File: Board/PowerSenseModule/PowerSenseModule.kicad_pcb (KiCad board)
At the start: 2 copper layers, 49 parts, among them J1 Conn_01x06_Male, J3 Programming Header, J4 Conn_01x02_Male, U1 TPS82150, U2 NCV2007x, U3 dsPIC33EV32GM102, U4 MCP2542FDxMF

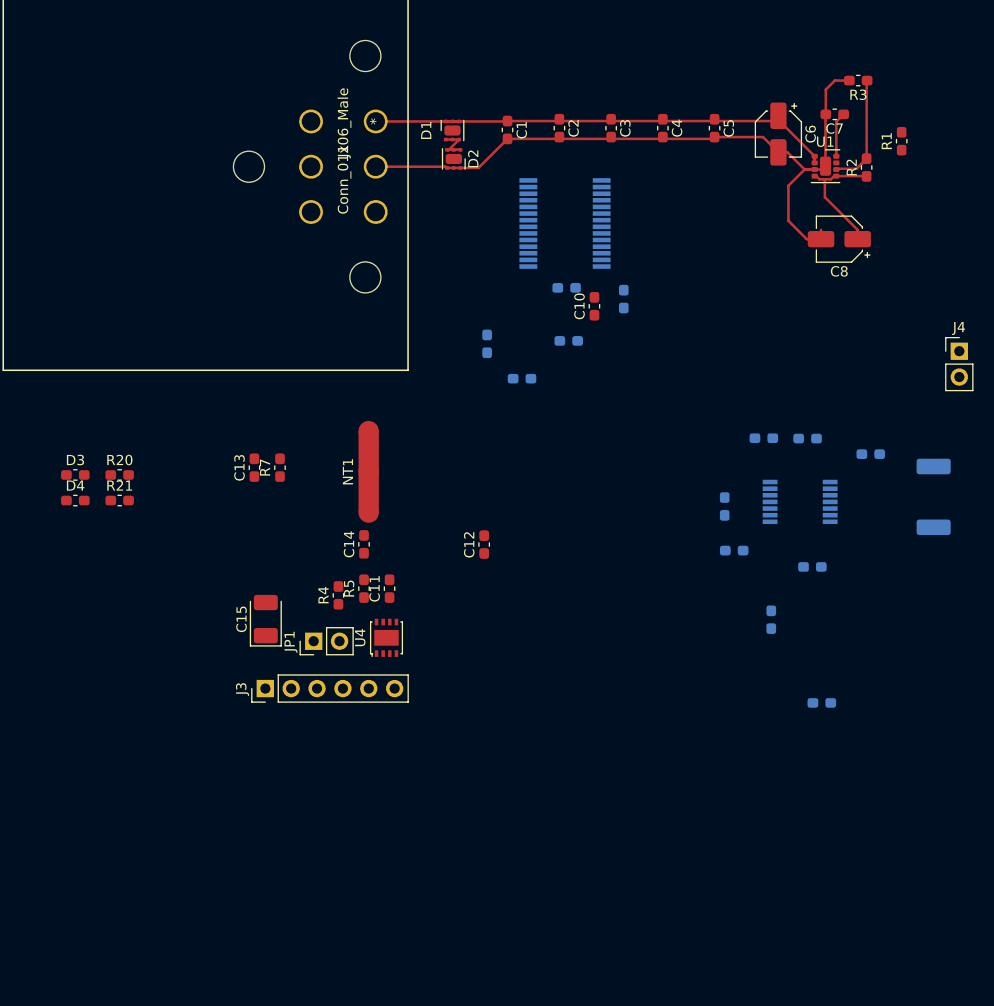
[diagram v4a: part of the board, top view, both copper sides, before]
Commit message: Added to PCB layout - Configurations Resistor / PIN 3 mapping
More of the PCB is laid out. Some mapping remains. Aside from that, what's left is the following, 
- Assuring PCB traces meet current limitations 
- Design review for optimizations for redesign. 
Alongside that, the configuration resistors do not seem to be connected to PIN 3 on the MCU.
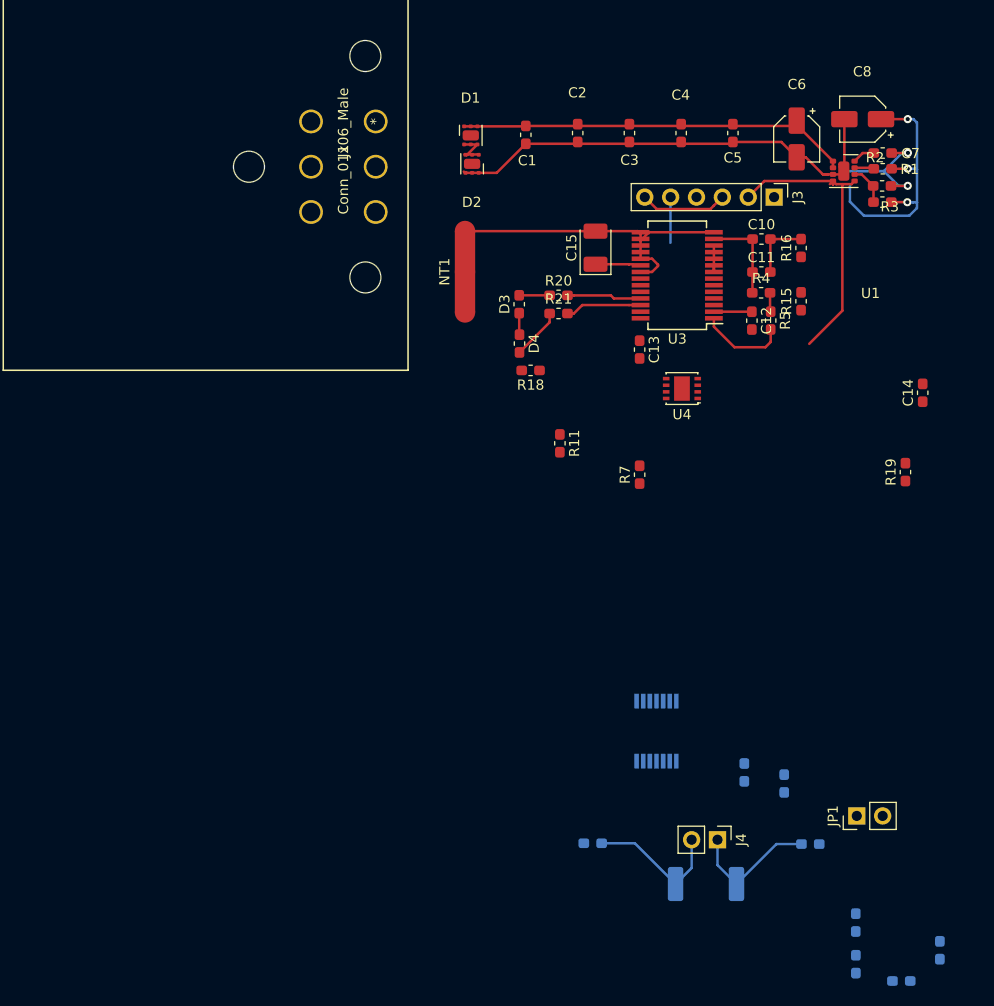
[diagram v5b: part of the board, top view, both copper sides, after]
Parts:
- R11, R15, R16, R18, R19, U3: moved to F.Cu
- moved R17 72.3 mm to (145.3, 168.6), turned to 180 degrees
- moved J3 69.5 mm to (132.8, 91.6), turned to 270 degrees
- moved C14 56.8 mm to (147.4, 110.8)
- moved JP1 56.0 mm to (140.9, 152.3)
- moved J4 53.5 mm to (127.2, 154.7), turned to 270 degrees
- moved R14 51.9 mm to (149.1, 165.5), turned to 90 degrees
- moved R4 51.0 mm to (131.5, 101.0), turned to 0 degrees
- moved C15 48.8 mm to (115.3, 96.5)
- moved R13 48.4 mm to (140.8, 162.8), turned to 270 degrees
- moved C11 48.0 mm to (131.6, 98.9), turned to 0 degrees
- moved R5 47.8 mm to (132.5, 103.7), turned to 270 degrees
- moved R21 46.8 mm to (111.6, 103.0)
- moved D3 46.7 mm to (107.8, 102.1), turned to 90 degrees
- moved R20 46.6 mm to (111.6, 101.2)
- moved D4 46.3 mm to (107.8, 106.0), turned to 270 degrees
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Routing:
- net +5V: track 12.6 -> 64.4 mm, vias 0 -> 3
- net GNDD: track 0.00 -> 51.6 mm
- net Net-(J4-Pad2): track 0.00 -> 14.0 mm
- net Net-(J4-Pad1): track 0.00 -> 13.2 mm
- net Net-(R5-Pad2): track 0.00 -> 8.67 mm
- net GND: track 68.1 -> 59.5 mm, vias 0 -> 2
- net +12V: track 46.8 -> 38.6 mm
- net Net-(R21-Pad2): track 0.00 -> 7.52 mm
- net Net-(R20-Pad2): track 0.00 -> 7.30 mm
- net Net-(R2-Pad2): track 11.1 -> 4.00 mm
- net Net-(D4-Pad2): track 0.00 -> 5.05 mm
- net Net-(J3-Pad5): track 0.00 -> 4.46 mm, vias 0 -> 1
- net Net-(C12-Pad1): track 0.00 -> 3.73 mm
- net Net-(C15-Pad1): track 0.00 -> 3.68 mm
- net Net-(D3-Pad2): track 0.00 -> 2.99 mm
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
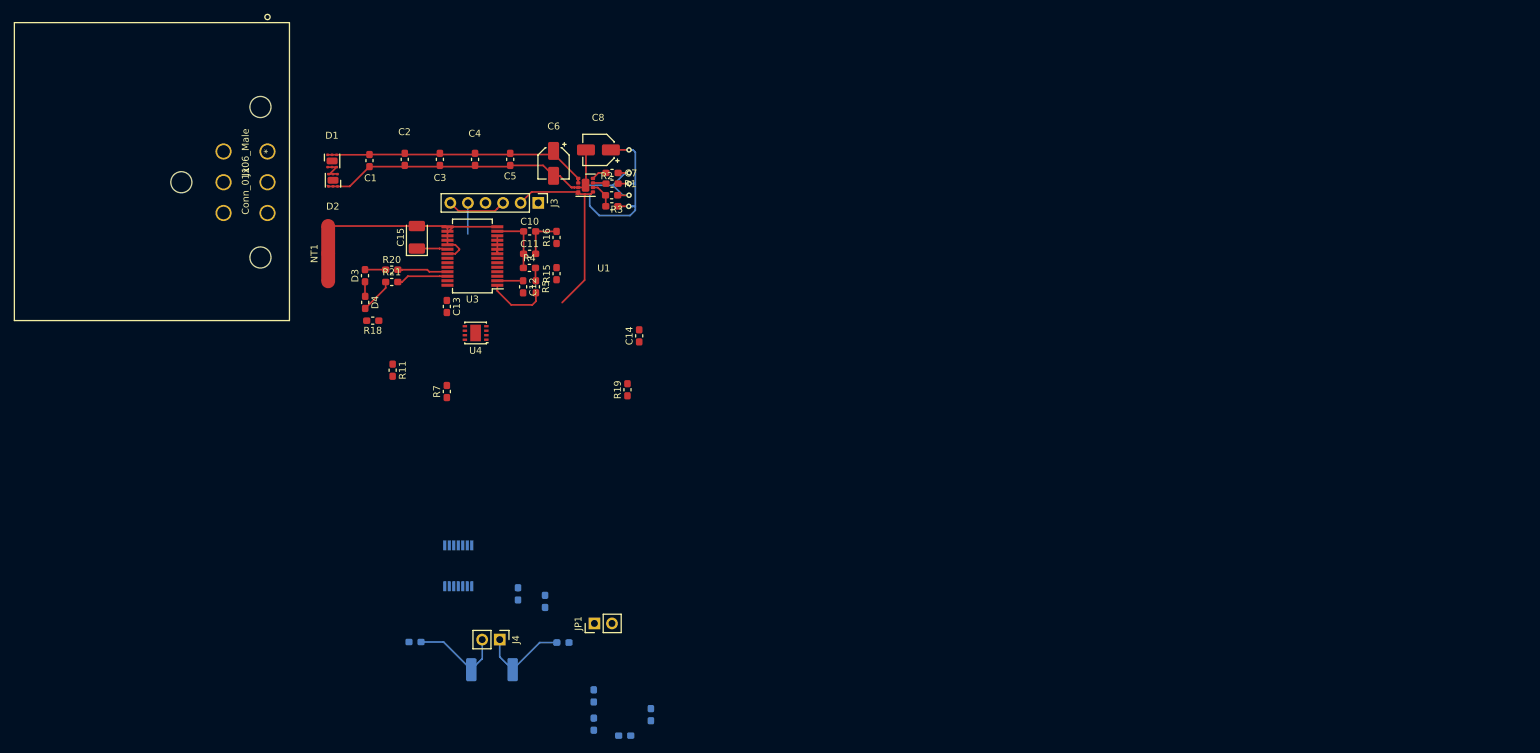
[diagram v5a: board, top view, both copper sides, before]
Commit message: Redesign/Configuration Resistors Fixed
Dimensions for PCB defined, might need to be extended for mounting. Rewiring being done to fit dimensions.
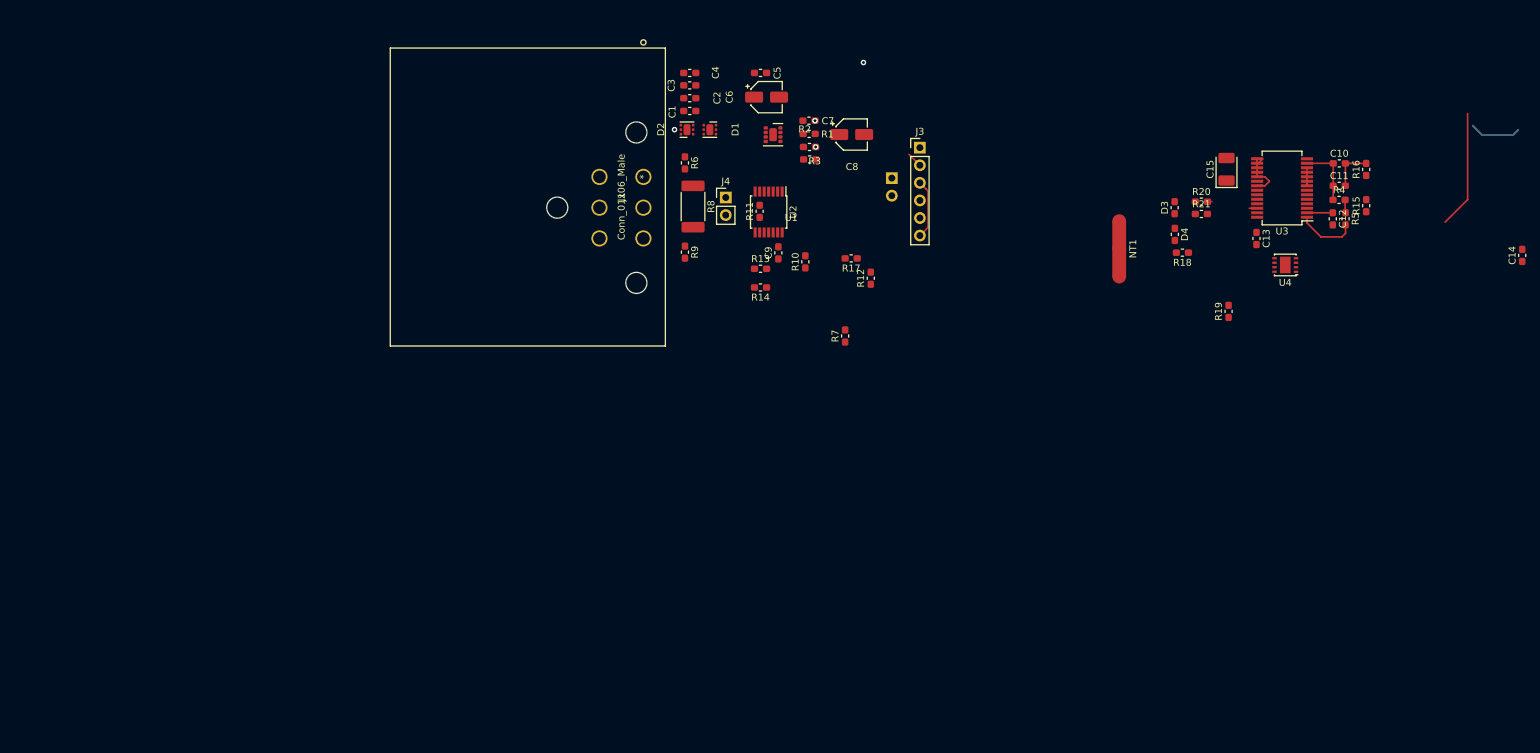
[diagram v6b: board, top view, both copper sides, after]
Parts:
- C9, R10, R12, R13, R14, R17, R6, R8, R9, U2: moved to F.Cu
- JP1: moved to B.Cu
- moved C14 128.1 mm to (275.0, 99.2)
- moved C11 117.4 mm to (248.5, 89.1)
- moved C12 117.4 mm to (247.6, 93.9)
- moved C15 117.4 mm to (232.3, 86.7)
- moved R18 117.4 mm to (225.9, 98.8)
- moved U4 117.4 mm to (240.8, 100.6)
- moved C10 117.4 mm to (248.6, 85.9)
- moved C13 117.4 mm to (236.6, 96.7)
- moved D3 117.4 mm to (224.8, 92.3)
- moved D4 117.4 mm to (224.8, 96.1)
- moved R15 117.4 mm to (252.4, 92.0)
- moved R16 117.4 mm to (252.4, 86.7)
- moved R20 117.4 mm to (228.6, 91.4)
- moved R21 117.4 mm to (228.6, 93.2)
- moved R4 117.4 mm to (248.5, 91.1)
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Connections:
- U3 pad 3: Net-(U3-Pad3) -> Net-(R15-Pad2)
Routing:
- net GND: track 59.5 -> 0.00 mm, vias 2 -> 16
- net +12V: track 38.6 -> 0.00 mm
- net +5V: track 64.4 -> 35.8 mm, vias 3 -> 0
- net GNDD: track 51.6 -> 26.2 mm
- net Net-(J4-Pad2): track 14.0 -> 0.00 mm
- net Net-(J4-Pad1): track 13.2 -> 0.00 mm
- net Net-(R20-Pad2): track 7.30 -> 0.01 mm
- net Net-(R21-Pad2): track 7.52 -> 1.12 mm
- net Net-(D4-Pad2): track 5.05 -> 0.00 mm
- net Net-(J3-Pad5): track 4.46 -> 0.00 mm
- net Net-(D1-Pad2): track 4.16 -> 0.00 mm
- net Net-(R2-Pad2): track 4.00 -> 0.00 mm
- net Net-(C15-Pad1): track 3.68 -> 0.00 mm
- net Net-(D3-Pad2): track 2.99 -> 0.01 mm
- net Net-(C7-Pad1): track 2.21 -> 0.00 mm
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
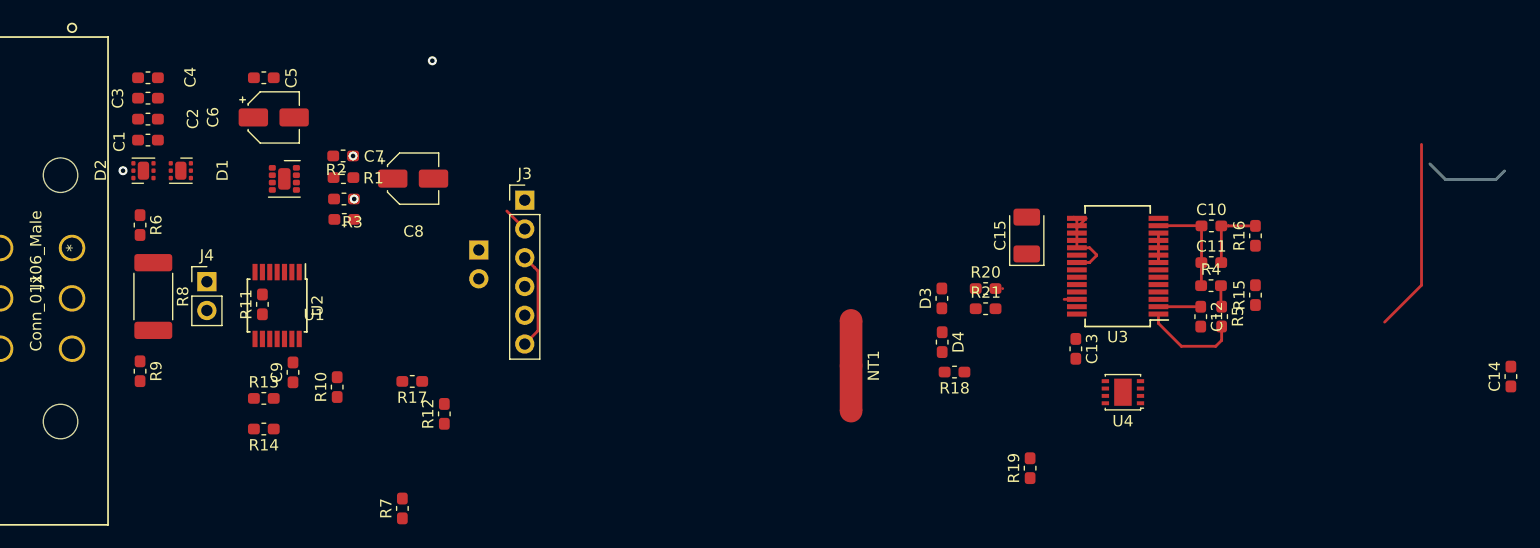
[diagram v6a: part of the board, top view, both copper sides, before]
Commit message: Redesign - Everything up top
This redesign has all components on top layer. Tracing is all that's left, along side labeling.
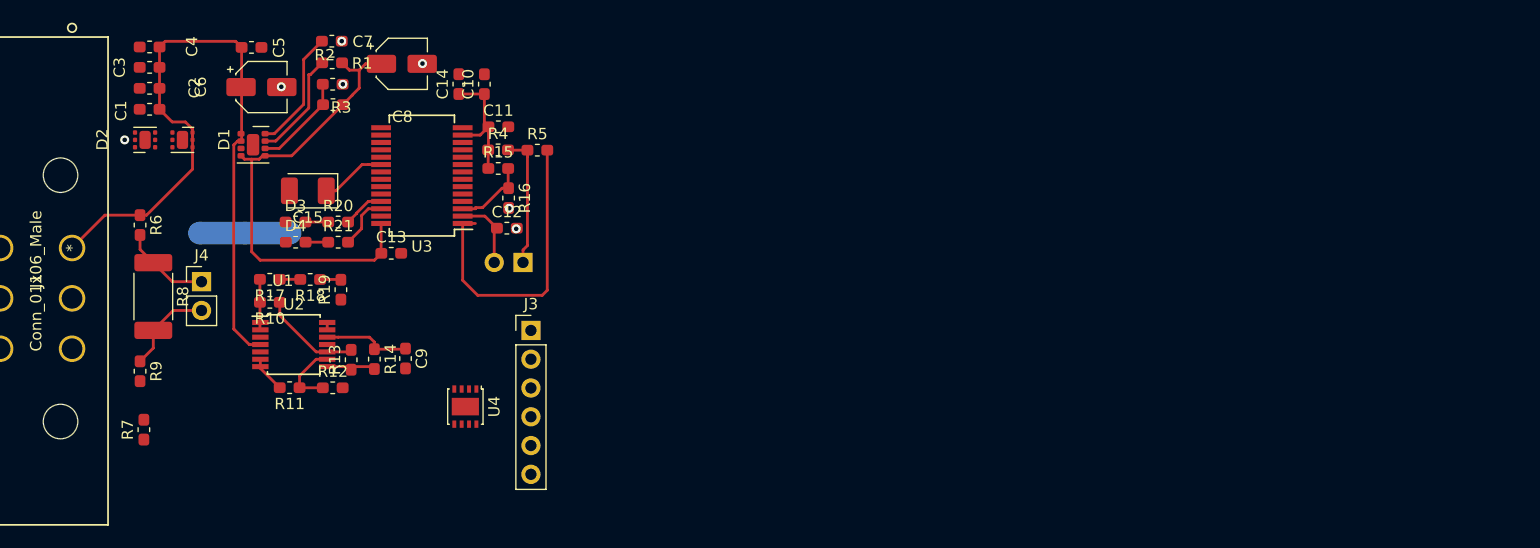
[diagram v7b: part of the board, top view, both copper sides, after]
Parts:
- NT1: moved to B.Cu
- moved C14 96.4 mm to (182.1, 73.4)
- moved R15 67.8 mm to (185.6, 80.8), turned to 0 degrees
- moved R16 66.0 mm to (186.5, 83.4), turned to 270 degrees
- moved C10 65.4 mm to (184.4, 73.4), turned to 90 degrees
- moved C11 64.1 mm to (185.6, 77.1)
- moved R4 64.1 mm to (185.6, 79.2)
- moved C15 63.6 mm to (168.8, 82.8), turned to 180 degrees
- moved R19 62.8 mm to (171.7, 91.5)
- moved R5 62.2 mm to (189.1, 79.2), turned to 0 degrees
- moved U3 61.9 mm to (178.9, 81.4)
- moved C12 61.7 mm to (186.4, 86.1), turned to 0 degrees
- moved C13 61.0 mm to (176.2, 88.3), turned to 0 degrees
- moved U4 58.1 mm to (182.7, 101.8), turned to 270 degrees
- moved D4 57.7 mm to (167.7, 87.3), turned to 0 degrees
- moved R18 57.5 mm to (169.0, 90.6)
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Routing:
- net +12V: track 0.00 -> 62.1 mm
- net GNDD: track 26.2 -> 0.08 mm, vias 0 -> 2
- net Net-(R5-Pad2): track 8.67 -> 26.7 mm
- net +5V: track 35.8 -> 53.2 mm
- net Net-(C7-Pad1): track 0.00 -> 10.7 mm
- net Net-(J3-Pad1): track 1.88 -> 11.9 mm
- net Net-(R1-Pad2): track 0.14 -> 9.77 mm
- net Net-(R10-Pad1): track 0.00 -> 8.87 mm
- net Net-(R2-Pad2): track 0.00 -> 8.53 mm
- net Net-(J4-Pad2): track 0.00 -> 8.20 mm
- net Net-(J4-Pad1): track 0.00 -> 7.88 mm
- net Net-(C9-Pad1): track 0.00 -> 7.74 mm
- net Net-(R15-Pad2): track 0.00 -> 6.61 mm
- net Net-(R11-Pad1): track 0.00 -> 6.15 mm
- net Net-(C15-Pad1): track 0.00 -> 5.80 mm
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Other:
- net class Power added: clearance 0.2, trace_width 18.77, via_dia 0.8, via_drill 0.4
